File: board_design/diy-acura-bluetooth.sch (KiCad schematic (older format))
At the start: 2 parts, among them P1 MBUS_CONN, P2 CONN_01X03

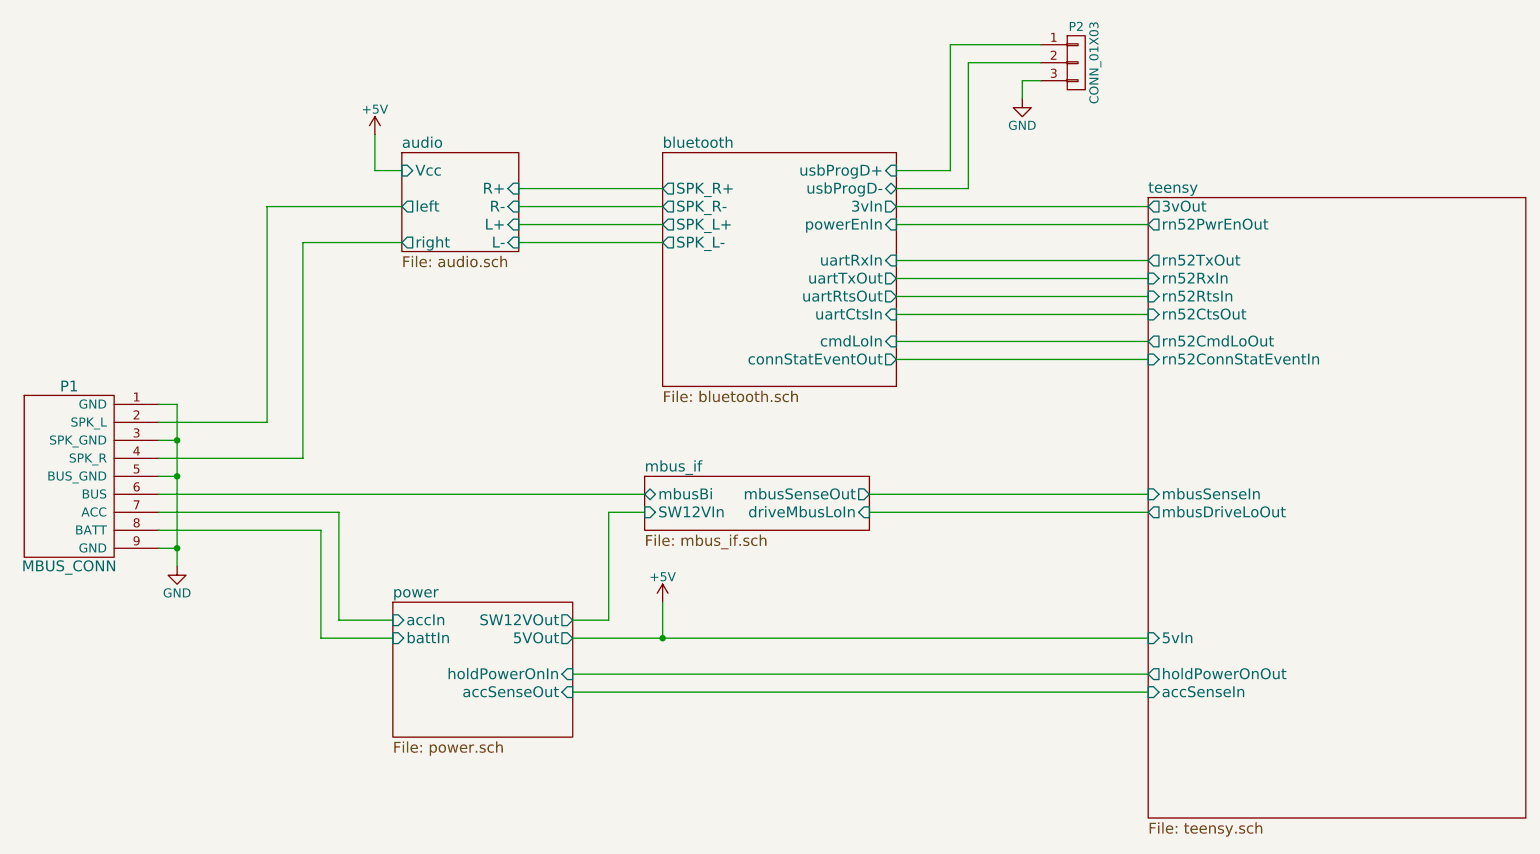
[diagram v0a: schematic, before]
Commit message: WIP commit before redoing layout for 0.5mm bit and before adding microphone port.
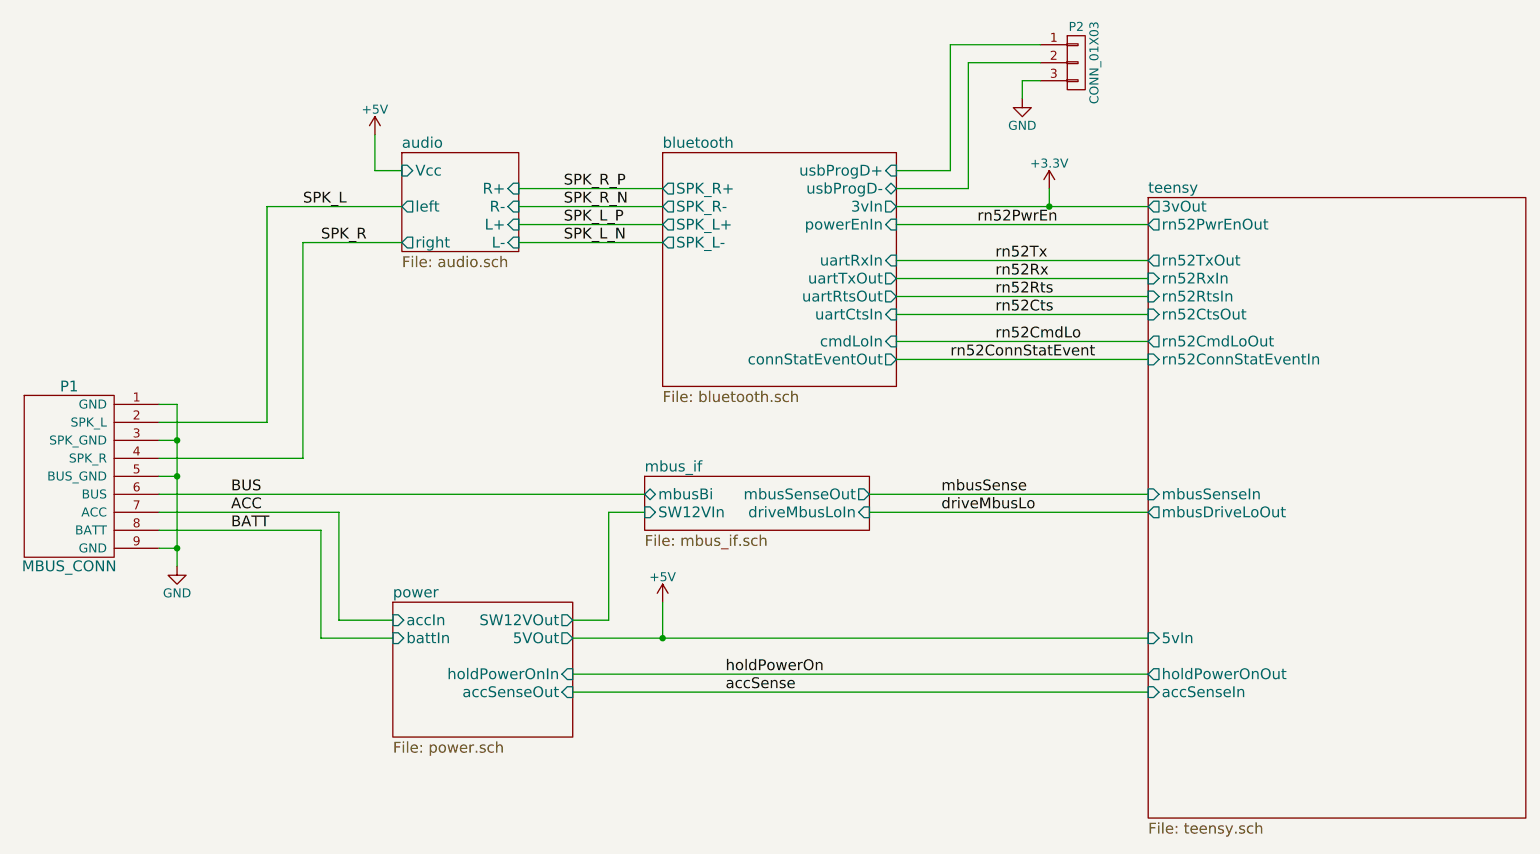
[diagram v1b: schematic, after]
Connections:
- net audio/left renamed SPK_L
- net audio/right renamed SPK_R
- net mbus_if/mbusBi renamed BUS
- net power/accIn renamed ACC
- net power/battIn renamed BATT
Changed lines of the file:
@@
 	6900 1800 5500 1800
 Wire Wire Line
-	6900 1700 5500 1700
+	5500 1700 6900 1700
 $Comp
 L CONN_01X03 P2
@@
 Wire Wire Line
 	6200 1000 6200 1100
+Text Label 2200 1700 0    60   ~ 0
+SPK_L
+Text Label 2300 1900 0    60   ~ 0
+SPK_R
+Text Label 1800 3400 0    60   ~ 0
+ACC
+Text Label 1800 3500 0    60   ~ 0
+BATT
+Text Label 1800 3300 0    60   ~ 0
+BUS
+Text Label 3650 1600 0    60   ~ 0
+SPK_R_P
+Text Label 3650 1700 0    60   ~ 0
+SPK_R_N
+Text Label 3650 1800 0    60   ~ 0
+SPK_L_P
+Text Label 3650 1900 0    60   ~ 0
+SPK_L_N
+Text Label 5750 3300 0    60   ~ 0
+mbusSense
+Text Label 5750 3400 0    60   ~ 0
+driveMbusLo
+Text Label 4550 4300 0    60   ~ 0
+holdPowerOn
+Text Label 4550 4400 0    60   ~ 0
+accSense
+$Comp
+L +3.3V #PWR05
+U 1 1 57047CF7
+P 6350 1600
+F 0 "#PWR05" H 6350 1450 50  0001 C CNN
+F 1 "+3.3V" H 6350 1740 50  0000 C CNN
+F 2 "" H 6350 1600 50  0000 C CNN
+F 3 "" H 6350 1600 50  0000 C CNN
+	1    6350 1600
+	1    0    0    -1
+$EndComp
+Wire Wire Line
+	6350 1600 6350 1700
+Connection ~ 6350 1700
+Text Label 5950 1800 0    60   ~ 0
+rn52PwrEn
+Text Label 6050 2000 0    60   ~ 0
+rn52Tx
+Text Label 6050 2100 0    60   ~ 0
+rn52Rx
+Text Label 6050 2200 0    60   ~ 0
+rn52Rts
+Text Label 6050 2300 0    60   ~ 0
+rn52Cts
+Text Label 6050 2450 0    60   ~ 0
+rn52CmdLo
+Text Label 5800 2550 0    60   ~ 0
+rn52ConnStatEvent
 $EndSCHEMATC
